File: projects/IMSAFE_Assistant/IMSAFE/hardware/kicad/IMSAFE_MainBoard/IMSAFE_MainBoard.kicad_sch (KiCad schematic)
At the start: 0 parts

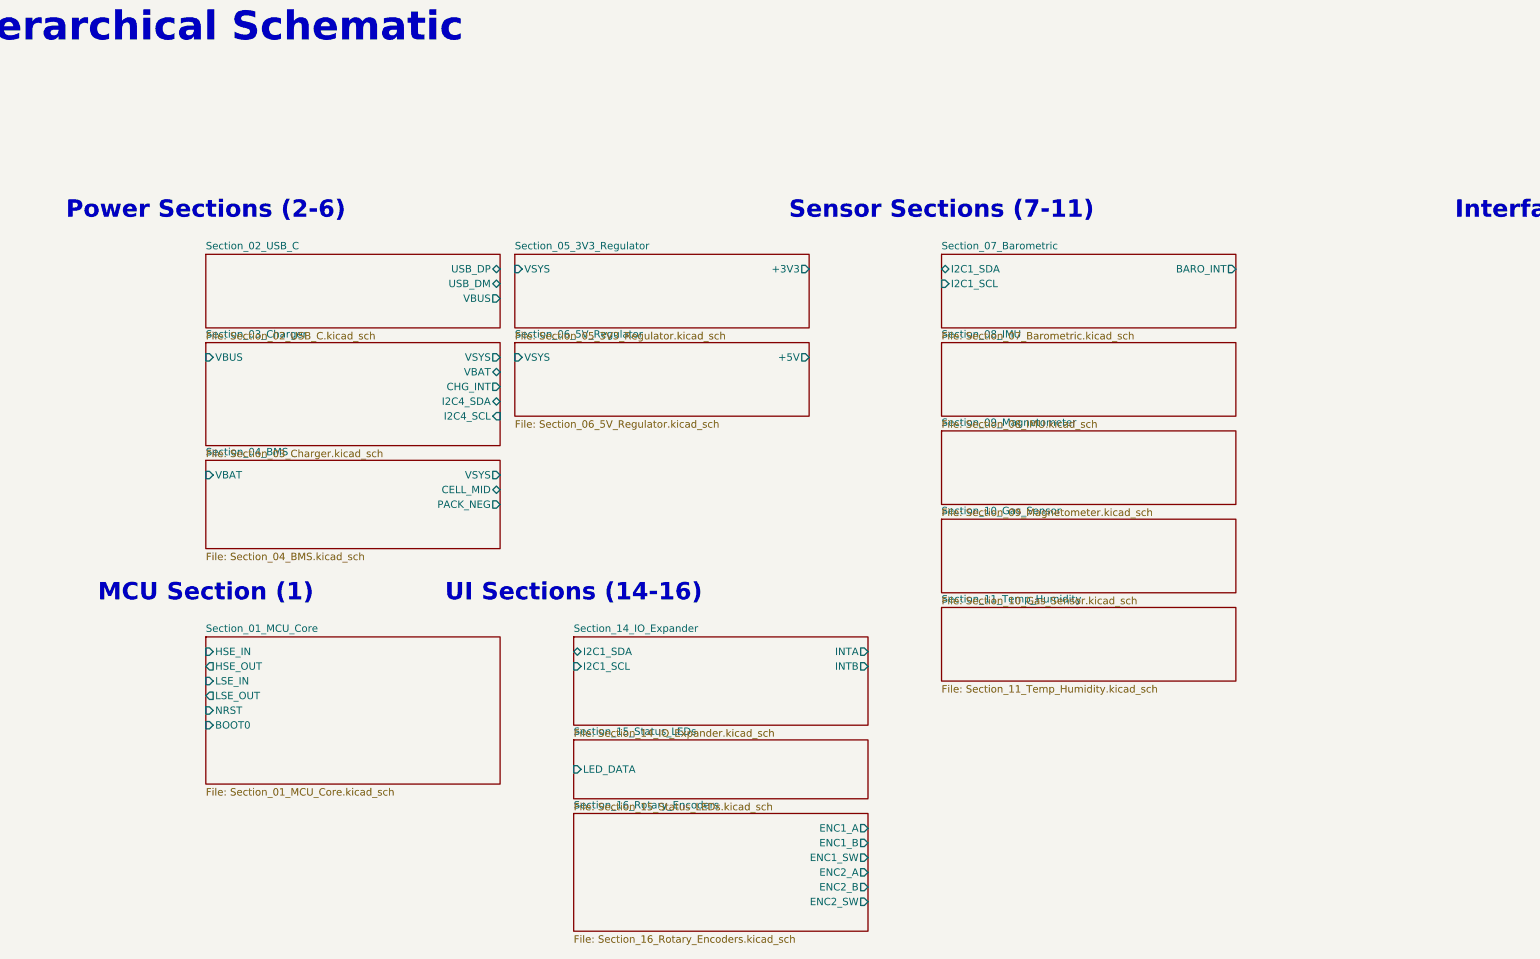
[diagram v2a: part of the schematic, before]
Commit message: Add power interconnections to root hierarchical schematic
- Add wires connecting sheet pins for VBUS, VSYS, VBAT power paths
- Add global labels for USB, I2C, interrupt, and encoder signals
- Connect USB-C VBUS output to Charger VBUS input
- Connect Charger VSYS to BMS, 3V3 Regulator, and 5V Regulator inputs
- Connect Charger VBAT to BMS battery input
- Route MCU crystal and control signals to global labels

ERC reduced from 174 errors to 150 errors in root schematic.
Remaining errors are in child schematics (unconnected pins, dangling wires).

Co-Authored-By: Claude Opus 4.5 <noreply@anthropic.com>
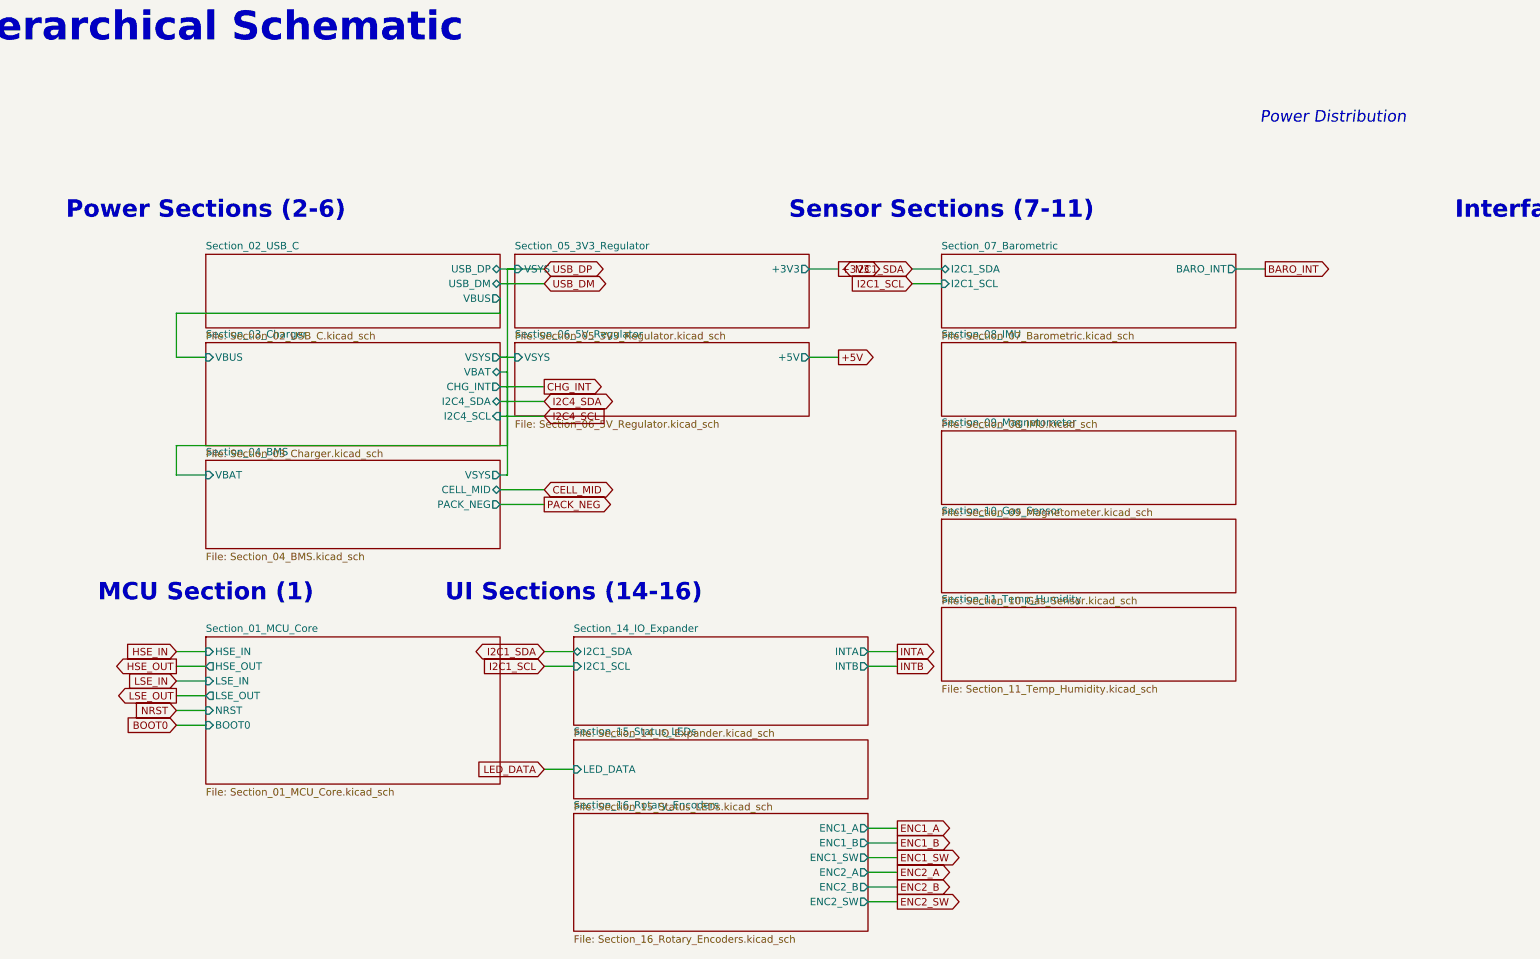
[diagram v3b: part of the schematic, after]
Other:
- note added: "Power Distribution"
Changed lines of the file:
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@@
 	(title_block
 		(title "IMSAFE MainBoard - Root")
-		(date "2026-01-28")
-		(rev "0.1")
+		(date "2026-01-29")
+		(rev "0.2")
 		(company "IMSAFE Project")
 		(comment 1 "STM32H747AG Based Aviation Instrument")
@@
 		(uuid "interface-label-001")
 	)
+	(text "Power Distribution"
+		(exclude_from_sim no)
+		(at 220 45 0)
+		(effects
+			(font
+				(size 2 2)
+				(italic yes)
+			)
+		)
+		(uuid "power-dist-label")
+	)
 	(sheet
 		(at 25.4 68.58)
@@
 		)
 	)
+	(wire (pts (xy 76.2 76.2) (xy 76.2 78.74)) (stroke (width 0) (type default)) (uuid "wire-vbus-1"))
+	(wire (pts (xy 76.2 78.74) (xy 20.32 78.74)) (stroke (width 0) (type default)) (uuid "wire-vbus-2"))
+	(wire (pts (xy 20.32 78.74) (xy 20.32 86.36)) (stroke (width 0) (type default)) (uuid "wire-vbus-3"))
+	(wire (pts (xy 20.32 86.36) (xy 25.4 86.36)) (stroke (width 0) (type default)) (uuid "wire-vbus-4"))
+	(wire (pts (xy 76.2 86.36) (xy 78.74 86.36)) (stroke (width 0) (type default)) (uuid "wire-vsys-5v"))
+	(wire (pts (xy 76.2 86.36) (xy 77.47 86.36)) (stroke (width 0) (type default)) (uuid "wire-vsys-j1"))
+	(wire (pts (xy 77.47 86.36) (xy 77.47 71.12)) (stroke (width 0) (type default)) (uuid "wire-vsys-up"))
+	(wire (pts (xy 77.47 71.12) (xy 78.74 71.12)) (stroke (width 0) (type default)) (uuid "wire-vsys-3v3"))
+	(wire (pts (xy 77.47 86.36) (xy 77.47 106.68)) (stroke (width 0) (type default)) (uuid "wire-vsys-down"))
+	(wire (pts (xy 77.47 106.68) (xy 76.2 106.68)) (stroke (width 0) (type default)) (uuid "wire-vsys-bms"))
+	(wire (pts (xy 76.2 88.9) (xy 77.47 88.9)) (stroke (width 0) (type default)) (uuid "wire-vbat-1"))
+	(wire (pts (xy 77.47 88.9) (xy 77.47 101.6)) (stroke (width 0) (type default)) (uuid "wire-vbat-2"))
+	(wire (pts (xy 77.47 101.6) (xy 20.32 101.6)) (stroke (width 0) (type default)) (uuid "wire-vbat-3"))
+	(wire (pts (xy 20.32 101.6) (xy 20.32 106.68)) (stroke (width 0) (type default)) (uuid "wire-vbat-4"))
+	(wire (pts (xy 20.32 106.68) (xy 25.4 106.68)) (stroke (width 0) (type default)) (uuid "wire-vbat-5"))
+	(wire (pts (xy 76.2 71.12) (xy 83.82 71.12)) (stroke (width 0) (type default)) (uuid "wire-usbdp"))
+	(wire (pts (xy 76.2 73.66) (xy 83.82 73.66)) (stroke (width 0) (type default)) (uuid "wire-usbdm"))
+	(wire (pts (xy 76.2 91.44) (xy 83.82 91.44)) (stroke (width 0) (type default)) (uuid "wire-chgint"))
+	(wire (pts (xy 76.2 93.98) (xy 83.82 93.98)) (stroke (width 0) (type default)) (uuid "wire-i2c4sda"))
+	(wire (pts (xy 76.2 96.52) (xy 83.82 96.52)) (stroke (width 0) (type default)) (uuid "wire-i2c4scl"))
+	(wire (pts (xy 76.2 109.22) (xy 83.82 109.22)) (stroke (width 0) (type default)) (uuid "wire-cellmid"))
+	(wire (pts (xy 76.2 111.76) (xy 83.82 111.76)) (stroke (width 0) (type default)) (uuid "wire-packneg"))
+	(wire (pts (xy 129.54 71.12) (xy 134.62 71.12)) (stroke (width 0) (type default)) (uuid "wire-3v3out"))
+	(wire (pts (xy 129.54 86.36) (xy 134.62 86.36)) (stroke (width 0) (type default)) (uuid "wire-5vout"))
+	(wire (pts (xy 152.4 71.12) (xy 147.32 71.12)) (stroke (width 0) (type default)) (uuid "wire-baro-sda"))
+	(wire (pts (xy 152.4 73.66) (xy 147.32 73.66)) (stroke (width 0) (type default)) (uuid "wire-baro-scl"))
+	(wire (pts (xy 203.2 71.12) (xy 208.28 71.12)) (stroke (width 0) (type default)) (uuid "wire-baro-int"))
+	(wire (pts (xy 88.9 137.16) (xy 83.82 137.16)) (stroke (width 0) (type default)) (uuid "wire-ioexp-sda"))
+	(wire (pts (xy 88.9 139.7) (xy 83.82 139.7)) (stroke (width 0) (type default)) (uuid "wire-ioexp-scl"))
+	(wire (pts (xy 139.7 137.16) (xy 144.78 137.16)) (stroke (width 0) (type default)) (uuid "wire-ioexp-inta"))
+	(wire (pts (xy 139.7 139.7) (xy 144.78 139.7)) (stroke (width 0) (type default)) (uuid "wire-ioexp-intb"))
+	(wire (pts (xy 88.9 157.48) (xy 83.82 157.48)) (stroke (width 0) (type default)) (uuid "wire-led-data"))
+	(wire (pts (xy 139.7 167.64) (xy 144.78 167.64)) (stroke (width 0) (type default)) (uuid "wire-enc1a"))
+	(wire (pts (xy 139.7 170.18) (xy 144.78 170.18)) (stroke (width 0) (type default)) (uuid "wire-enc1b"))
+	(wire (pts (xy 139.7 172.72) (xy 144.78 172.72)) (stroke (width 0) (type default)) (uuid "wire-enc1sw"))
+	(wire (pts (xy 139.7 175.26) (xy 144.78 175.26)) (stroke (width 0) (type default)) (uuid "wire-enc2a"))
+	(wire (pts (xy 139.7 177.8) (xy 144.78 177.8)) (stroke (width 0) (type default)) (uuid "wire-enc2b"))
+	(wire (pts (xy 139.7 180.34) (xy 144.78 180.34)) (stroke (width 0) (type default)) (uuid "wire-enc2sw"))
+	(wire (pts (xy 25.4 137.16) (xy 20.32 137.16)) (stroke (width 0) (type default)) (uuid "wire-mcu-hsein"))
+	(wire (pts (xy 25.4 139.7) (xy 20.32 139.7)) (stroke (width 0) (type default)) (uuid "wire-mcu-hseout"))
+	(wire (pts (xy 25.4 142.24) (xy 20.32 142.24)) (stroke (width 0) (type default)) (uuid "wire-mcu-lsein"))
+	(wire (pts (xy 25.4 144.78) (xy 20.32 144.78)) (stroke (width 0) (type default)) (uuid "wire-mcu-lseout"))
+	(wire (pts (xy 25.4 147.32) (xy 20.32 147.32)) (stroke (width 0) (type default)) (uuid "wire-mcu-nrst"))
+	(wire (pts (xy 25.4 149.86) (xy 20.32 149.86)) (stroke (width 0) (type default)) (uuid "wire-mcu-boot0"))
+	(global_label "USB_DP" (shape bidirectional) (at 83.82 71.12 0) (fields_autoplaced yes)
+		(effects (font (size 1.27 1.27)) (justify left))
+		(uuid "gl-usbdp")
+	)
+	(global_label "USB_DM" (shape bidirectional) (at 83.82 73.66 0) (fields_autoplaced yes)
+		(effects (font (size 1.27 1.27)) (justify left))
+		(uuid "gl-usbdm")
+	)
+	(global_label "CHG_INT" (shape output) (at 83.82 91.44 0) (fields_autoplaced yes)
+		(effects (font (size 1.27 1.27)) (justify left))
+		(uuid "gl-chgint")
+	)
+	(global_label "I2C4_SDA" (shape bidirectional) (at 83.82 93.98 0) (fields_autoplaced yes)
+		(effects (font (size 1.27 1.27)) (justify left))
+		(uuid "gl-i2c4sda")
+	)
+	(global_label "I2C4_SCL" (shape input) (at 83.82 96.52 0) (fields_autoplaced yes)
+		(effects (font (size 1.27 1.27)) (justify left))
+		(uuid "gl-i2c4scl")
+	)
+	(global_label "CELL_MID" (shape bidirectional) (at 83.82 109.22 0) (fields_autoplaced yes)
+		(effects (font (size 1.27 1.27)) (justify left))
+		(uuid "gl-cellmid")
+	)
+	(global_label "PACK_NEG" (shape output) (at 83.82 111.76 0) (fields_autoplaced yes)
+		(effects (font (size 1.27 1.27)) (justify left))
+		(uuid "gl-packneg")
+	)
+	(global_label "+3V3" (shape output) (at 134.62 71.12 0) (fields_autoplaced yes)
+		(effects (font (size 1.27 1.27)) (justify left))
+		(uuid "gl-3v3")
+	)
+	(global_label "+5V" (shape output) (at 134.62 86.36 0) (fields_autoplaced yes)
+		(effects (font (size 1.27 1.27)) (justify left))
+		(uuid "gl-5v")
+	)
+	(global_label "I2C1_SDA" (shape bidirectional) (at 147.32 71.12 180) (fields_autoplaced yes)
+		(effects (font (size 1.27 1.27)) (justify right))
+		(uuid "gl-i2c1sda-baro")
+	)
+	(global_label "I2C1_SCL" (shape input) (at 147.32 73.66 180) (fields_autoplaced yes)
+		(effects (font (size 1.27 1.27)) (justify right))
+		(uuid "gl-i2c1scl-baro")
+	)
+	(global_label "BARO_INT" (shape output) (at 208.28 71.12 0) (fields_autoplaced yes)
+		(effects (font (size 1.27 1.27)) (justify left))
+		(uuid "gl-baroint")
+	)
+	(global_label "I2C1_SDA" (shape bidirectional) (at 83.82 137.16 180) (fields_autoplaced yes)
+		(effects (font (size 1.27 1.27)) (justify right))
+		(uuid "gl-i2c1sda-ioexp")
+	)
+	(global_label "I2C1_SCL" (shape input) (at 83.82 139.7 180) (fields_autoplaced yes)
+		(effects (font (size 1.27 1.27)) (justify right))
+		(uuid "gl-i2c1scl-ioexp")
+	)
+	(global_label "INTA" (shape output) (at 144.78 137.16 0) (fields_autoplaced yes)
+		(effects (font (size 1.27 1.27)) (justify left))
+		(uuid "gl-inta")
+	)
+	(global_label "INTB" (shape output) (at 144.78 139.7 0) (fields_autoplaced yes)
+		(effects (font (size 1.27 1.27)) (justify left))
+		(uuid "gl-intb")
+	)
+	(global_label "LED_DATA" (shape input) (at 83.82 157.48 180) (fields_autoplaced yes)
+		(effects (font (size 1.27 1.27)) (justify right))
+		(uuid "gl-leddata")
+	)
+	(global_label "ENC1_A" (shape output) (at 144.78 167.64 0) (fields_autoplaced yes)
+		(effects (font (size 1.27 1.27)) (justify left))
+		(uuid "gl-enc1a")
+	)
+	(global_label "ENC1_B" (shape output) (at 144.78 170.18 0) (fields_autoplaced yes)
+		(effects (font (size 1.27 1.27)) (justify left))
+		(uuid "gl-enc1b")
+	)
+	(global_label "ENC1_SW" (shape output) (at 144.78 172.72 0) (fields_autoplaced yes)
+		(effects (font (size 1.27 1.27)) (justify left))
+		(uuid "gl-enc1sw")
+	)
+	(global_label "ENC2_A" (shape output) (at 144.78 175.26 0) (fields_autoplaced yes)
+		(effects (font (size 1.27 1.27)) (justify left))
+		(uuid "gl-enc2a")
+	)
+	(global_label "ENC2_B" (shape output) (at 144.78 177.8 0) (fields_autoplaced yes)
+		(effects (font (size 1.27 1.27)) (justify left))
+		(uuid "gl-enc2b")
+	)
+	(global_label "ENC2_SW" (shape output) (at 144.78 180.34 0) (fields_autoplaced yes)
+		(effects (font (size 1.27 1.27)) (justify left))
+		(uuid "gl-enc2sw")
+	)
+	(global_label "HSE_IN" (shape input) (at 20.32 137.16 180) (fields_autoplaced yes)
+		(effects (font (size 1.27 1.27)) (justify right))
+		(uuid "gl-hsein")
+	)
+	(global_label "HSE_OUT" (shape output) (at 20.32 139.7 180) (fields_autoplaced yes)
+		(effects (font (size 1.27 1.27)) (justify right))
+		(uuid "gl-hseout")
+	)
+	(global_label "LSE_IN" (shape input) (at 20.32 142.24 180) (fields_autoplaced yes)
+		(effects (font (size 1.27 1.27)) (justify right))
+		(uuid "gl-lsein")
+	)
+	(global_label "LSE_OUT" (shape output) (at 20.32 144.78 180) (fields_autoplaced yes)
+		(effects (font (size 1.27 1.27)) (justify right))
+		(uuid "gl-lseout")
+	)
+	(global_label "NRST" (shape input) (at 20.32 147.32 180) (fields_autoplaced yes)
+		(effects (font (size 1.27 1.27)) (justify right))
+		(uuid "gl-nrst")
+	)
+	(global_label "BOOT0" (shape input) (at 20.32 149.86 180) (fields_autoplaced yes)
+		(effects (font (size 1.27 1.27)) (justify right))
+		(uuid "gl-boot0")
+	)
 	(sheet_instances
